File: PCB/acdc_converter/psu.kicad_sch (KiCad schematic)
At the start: 64 parts, among them J1 MAINS L N PE, J2 9V OUT, K1 G6K-2F-Y DC12, K2 G6K-2F-Y DC12, Q1 2N7002, U1 LM317, U2 LM317, U3 L78L12, U4 CD4060B, U5 LT3045

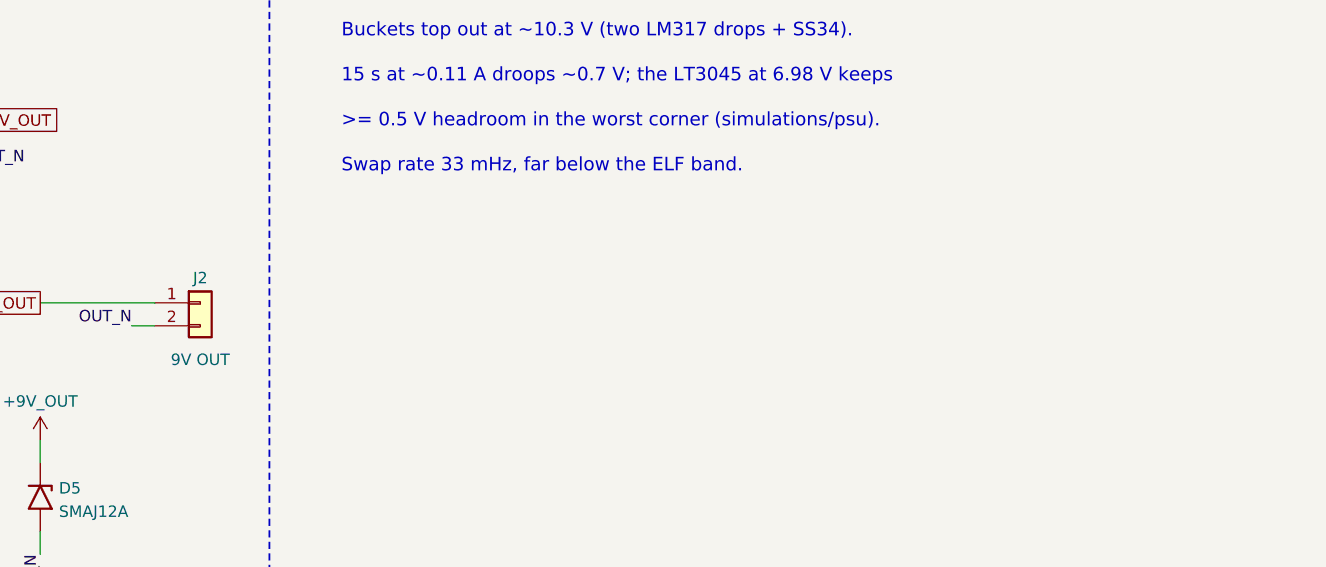
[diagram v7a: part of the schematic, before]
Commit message: AES3 source resistors 22 ohm for a 111 ohm source; tidy schematics and assembly drawings
- R412/R413 2 x 39 -> 2 x 22 ohm (Vishay TNPW060322R0BEEA, anti-sulfur): the
  CS8406 drivers are 33.5 ohm each at VL = 3.3 V, so 2 x 39 gave a 145 ohm
  source, outside AES3's 110 ohm +-20 %. The schematic note had used the 5 V
  figure and mis-added it.
- AES3 sheet: transformer flipped (kicadgen gains mirror='x') and wired straight
  to R412/R413/C405 and the RJ45, no more touching AES_HOT/AES_COLD labels.
- Stale S/PDIF and 9 V wording out of the sheets and BOM: DC input block reads
  6.98-15 V, J101 'DC IN', PSU J2 'DC OUT', reset button and clock branch say
  AES3; the legacy +9V / +9V_OUT net names are explained on the sheets.
- PSU root sheet gets the same power-path / board summary as the amplifier.
- Assembly drawings: fab-layer copies of the references removed wherever the
  silk reference shows (KiCad 9 texts cannot be hidden), so each part is named
  once; J201/J202 (no silk on the guard island) get theirs beside the part.
- BOM totals +0.14 EUR (502.15 ex VAT reference build, 407.22 recommended).

Co-Authored-By: Claude Opus 5.5 <noreply@anthropic.com>
Claude-Session: https://claude.ai/code/session_01RsM1DhHhY1tSr2aHjVygSC
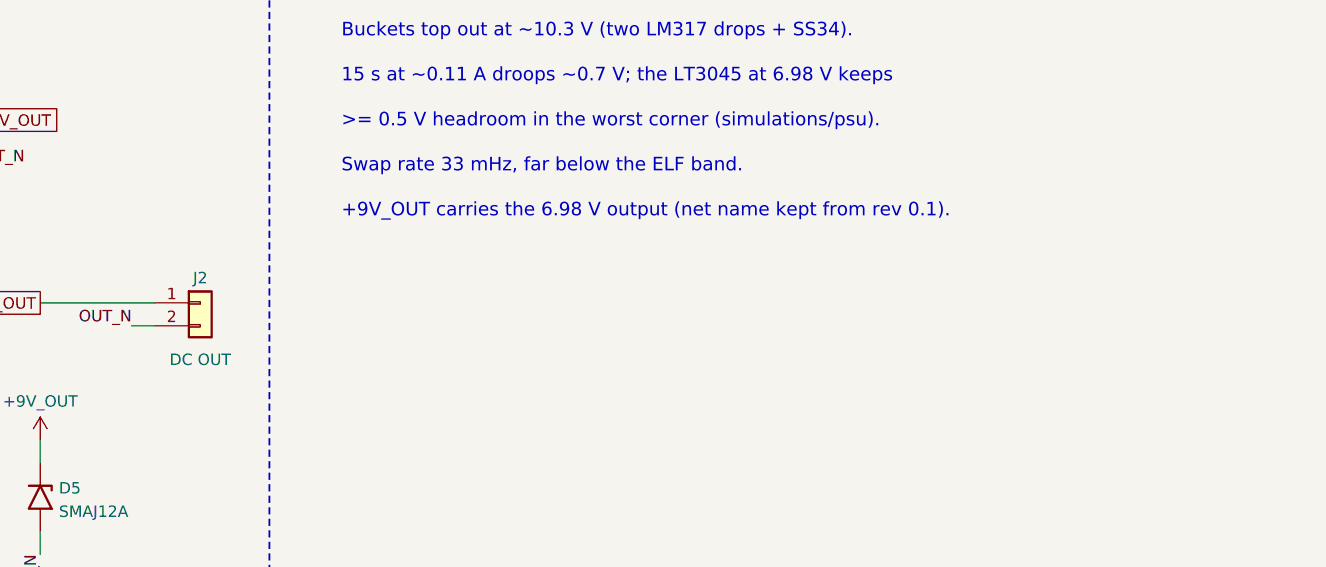
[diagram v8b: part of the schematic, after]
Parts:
- J2: value 9V OUT -> DC OUT
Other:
- note added: "+9V_OUT carries the 6.98 V output (net name kept from rev 0.1)."
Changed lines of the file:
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@@
 			)
 		)
-		(property "Value" "9V OUT"
+		(property "Value" "DC OUT"
 			(at 274.32 247.61 0)
 			(effects
@@
 		(effects
 			(font
+				(size 1.5 1.5)
+			)
+			(justify left bottom)
+		)
+	)
+	(text "+9V_OUT carries the 6.98 V output (net name kept from rev 0.1)."
+		(exclude_from_sim no)
+		(at 290 232 0)
+		(effects
+			(font
